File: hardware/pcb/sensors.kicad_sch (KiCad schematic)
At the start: 31 parts, among them J4 4-20mA_1, J5 4-20mA_2, J6 DS18B20, J7 Spare, Q2 BSS123, U9 ADS1115

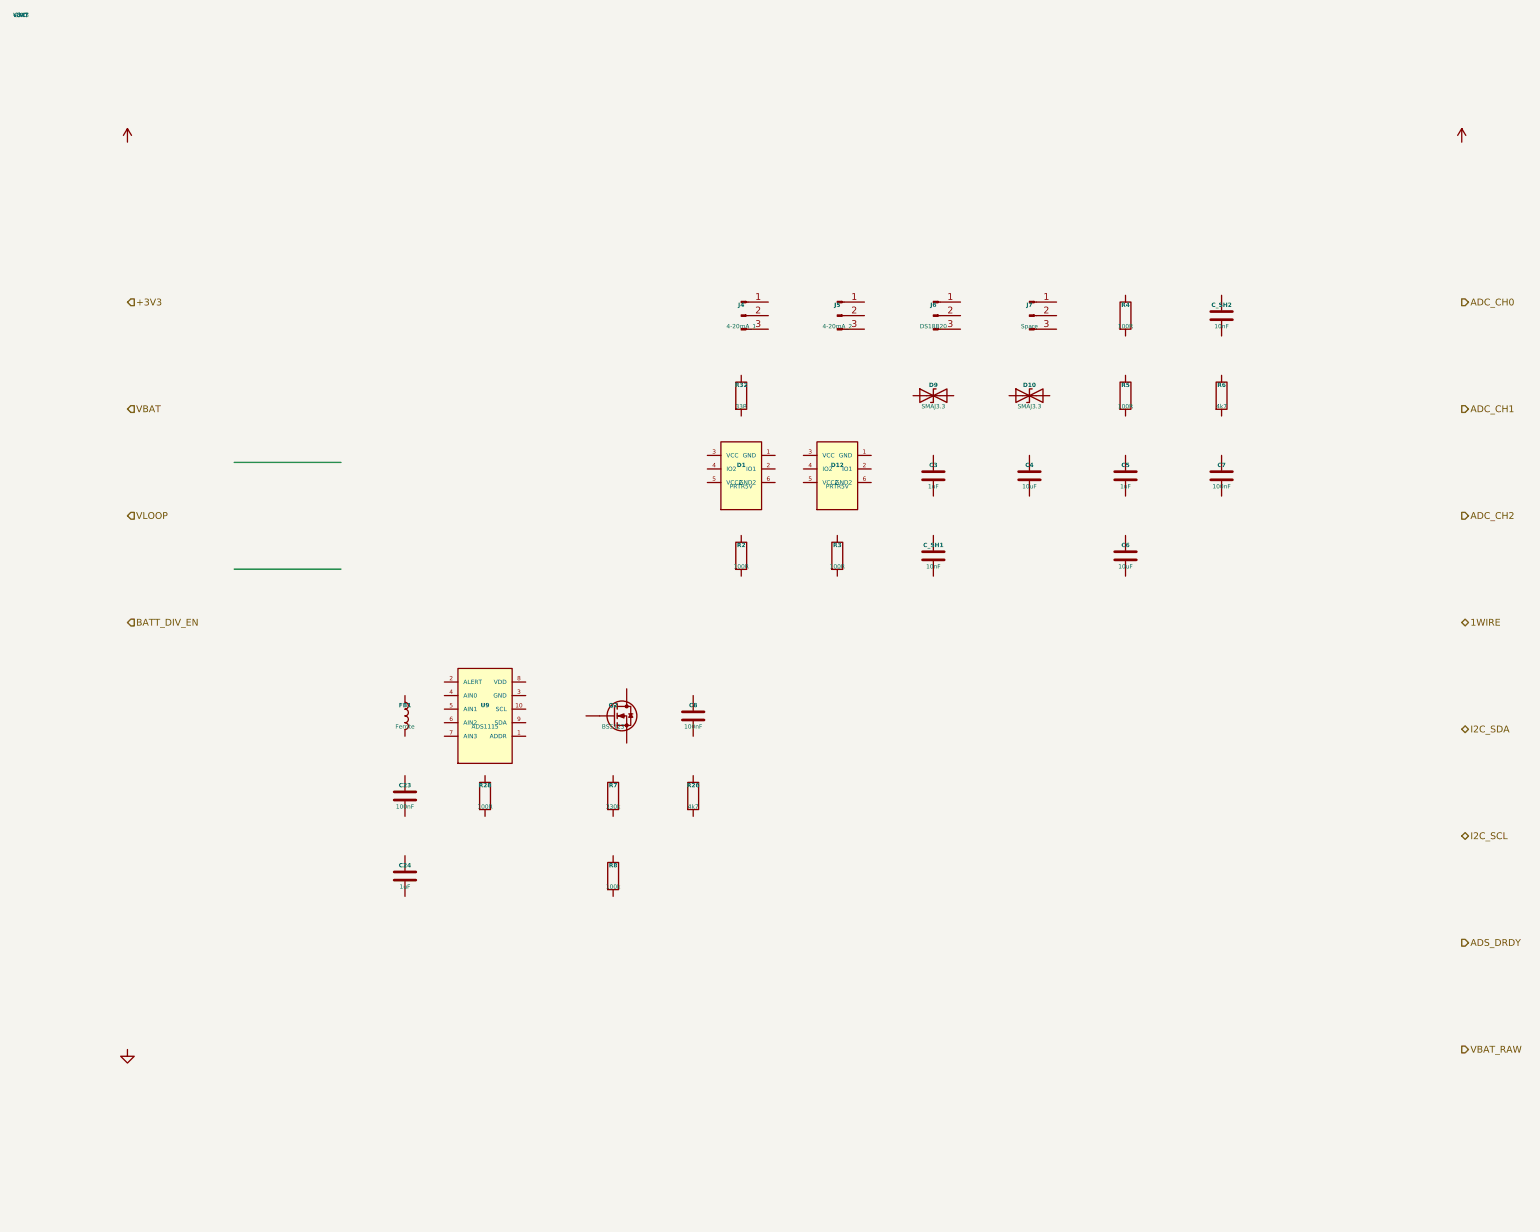
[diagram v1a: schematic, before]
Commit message: fix(sch): eliminate all structural ERC violations in hierarchical schematic
Three root causes fixed in generate_kicad.py:

1. Left-side sheet pins used angle=0 — kicad-cli upgrade snapped them to
   the right border, colliding with right-side pins and causing
   multiple_net_names and unconnected_wire_endpoint. Fixed: px==0 pins
   now use angle=180 (outward-left), px>0 pins keep angle=0.

2. Subsheet hierarchical labels and power symbols were at off-grid
   positions (20 mm, 50 mm, 70 mm, …). Replaced with 1.27 mm-aligned
   values (25.4, 50.8, 63.5, … multiples of 500 mil).

3. _remap_positions() produced arbitrary floats. Added _snap() that
   rounds every remapped coordinate to the nearest 1.27 mm grid point,
   eliminating component-pin endpoint_off_grid violations.

Also: paper size bumped A3 → A2 (layout reaches y ≈ 407 mm, exceeding
A3 height of 297 mm). SHEETS definition pinned to 1.27 mm-aligned
origins and heights; MCU left-side pins reordered to match power
right-side y-levels for direct horizontal wires.

ERC result: 588 → 404 violations.
Eliminated: endpoint_off_grid (−129), unconnected_wire_endpoint (−4),
wire_dangling (−2), multiple_net_names (−1).
Remaining 404 are structural (pin_not_connected, label_dangling) that
require full intra-sheet wiring — not addressable by the generator alone.

Netlist unchanged: 118 refs, 34 nets.

Co-Authored-By: Claude Sonnet 4.6 <noreply@anthropic.com>
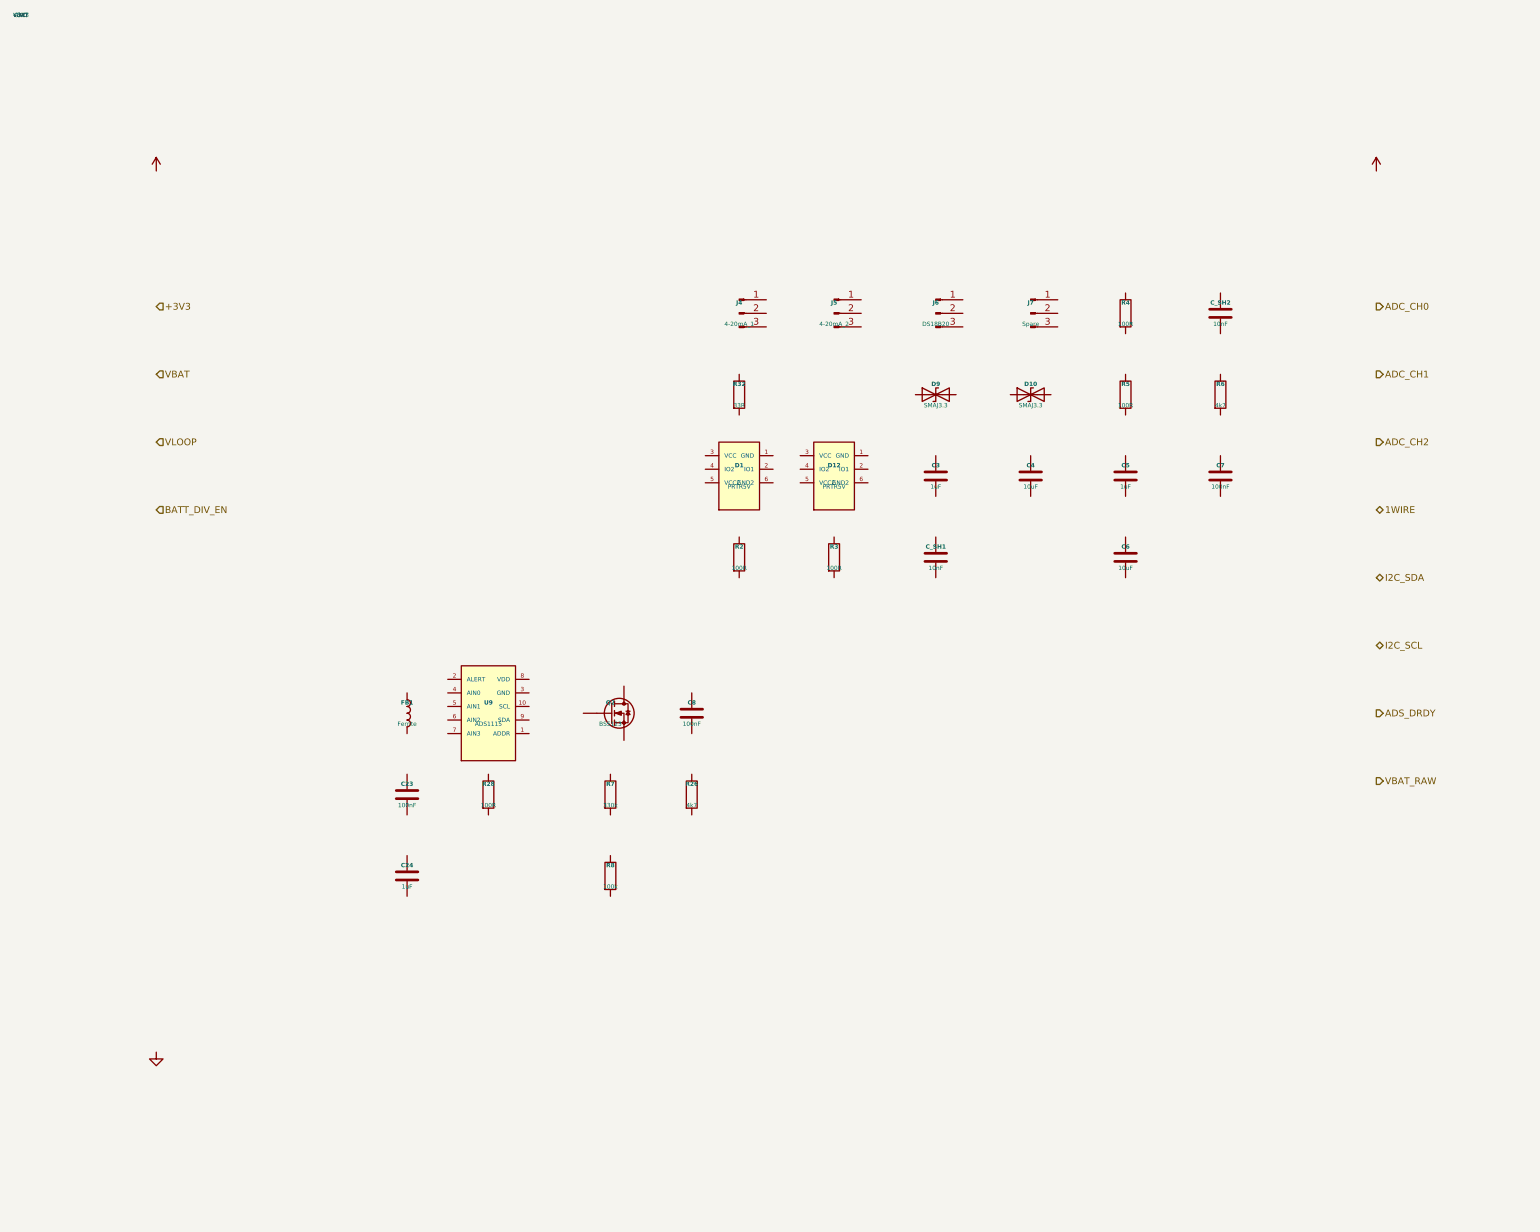
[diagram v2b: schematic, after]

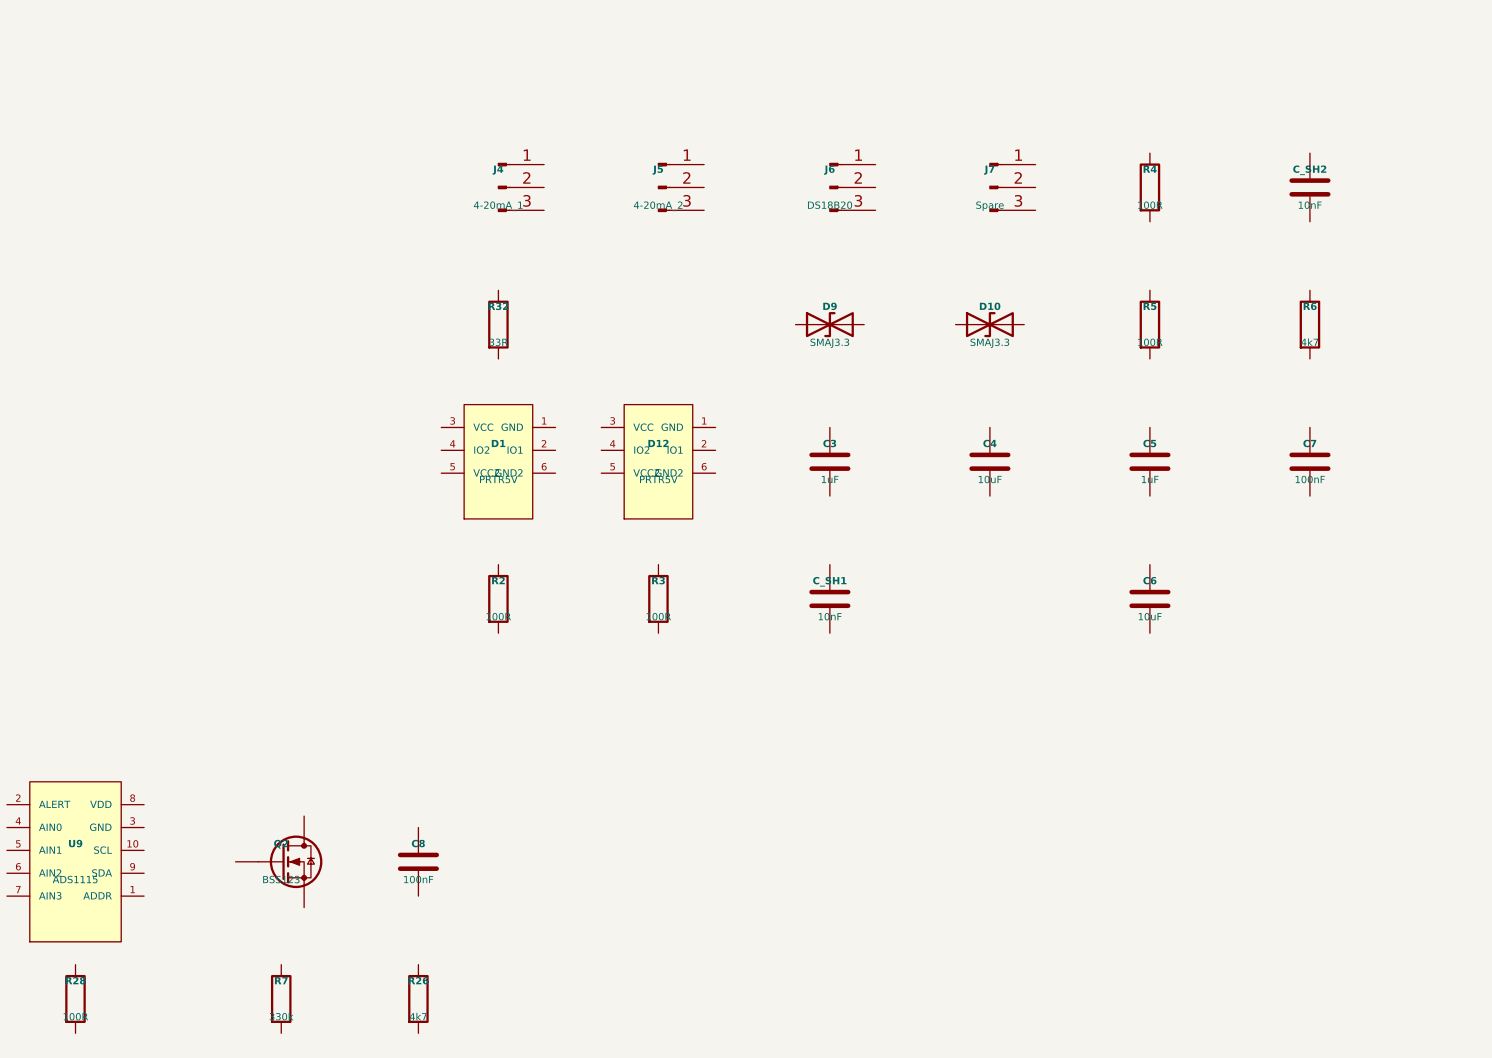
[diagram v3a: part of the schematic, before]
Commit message: hw(pcb): fresh-start PCB — fix 4 critical schematic gaps, add wiring/placement docs
Archive old auto-generated PCB to hardware/pcb_old/. Start clean hardware/pcb/
with reference-only design documents for manual KiCad layout.

Critical electrical fixes:
- Add R_FBH (560kΩ) and R_FBL (124kΩ) symbols to power.kicad_sch — AP63205WU
  was missing its FB divider entirely; without it VOUT floats to rail and destroys
  the ESP32 on first power-on. Sets VOUT = 3.31V.
- Add R_DRDY (4.7kΩ) symbol to sensors.kicad_sch — ADS1115 ALERT/DRDY is
  open-drain and required an external pull-up; firmware was missing edges
  intermittently (root cause of bug fixed in adf7101).
- Add C_BST (100nF) symbol to power.kicad_sch — MT3608B BST→SW bootstrap
  cap is mandatory for gate driver; was ambiguous/missing.
- Add C_BUCK (10µF 0805) symbol to power.kicad_sch — AP63205WU primary output
  filter cap was absent from schematic.
- R33 already corrected from 604kΩ → 590kΩ (CN3722 CV 8.48V → 8.31V, safe for 2S).

New reference documents:
- bom_footprints.md — full BOM with KiCad 10 footprints, LCSC codes, PCBWay notes
- placement_constraints.md — must-be-near/apart rules from datasheets
- schematic_connections.md — net-by-net pin connectivity (authoritative wiring ref
  because schematic has symbols but zero wire connections yet)
- kicad_guide_eli5.md — step-by-step KiCad 10 setup guide including scripting console
- kicad_place_script.py — PCB editor scripting console auto-placement script
- senior_review_2026-05-25.md — senior reviewer report (BLOCKED, 4 CRITICAL)

CLAUDE.md: add electrical correctness gate to /improve cycle to catch missing
companion passives before tape-out.

Co-Authored-By: Claude Sonnet 4.6 <noreply@anthropic.com>
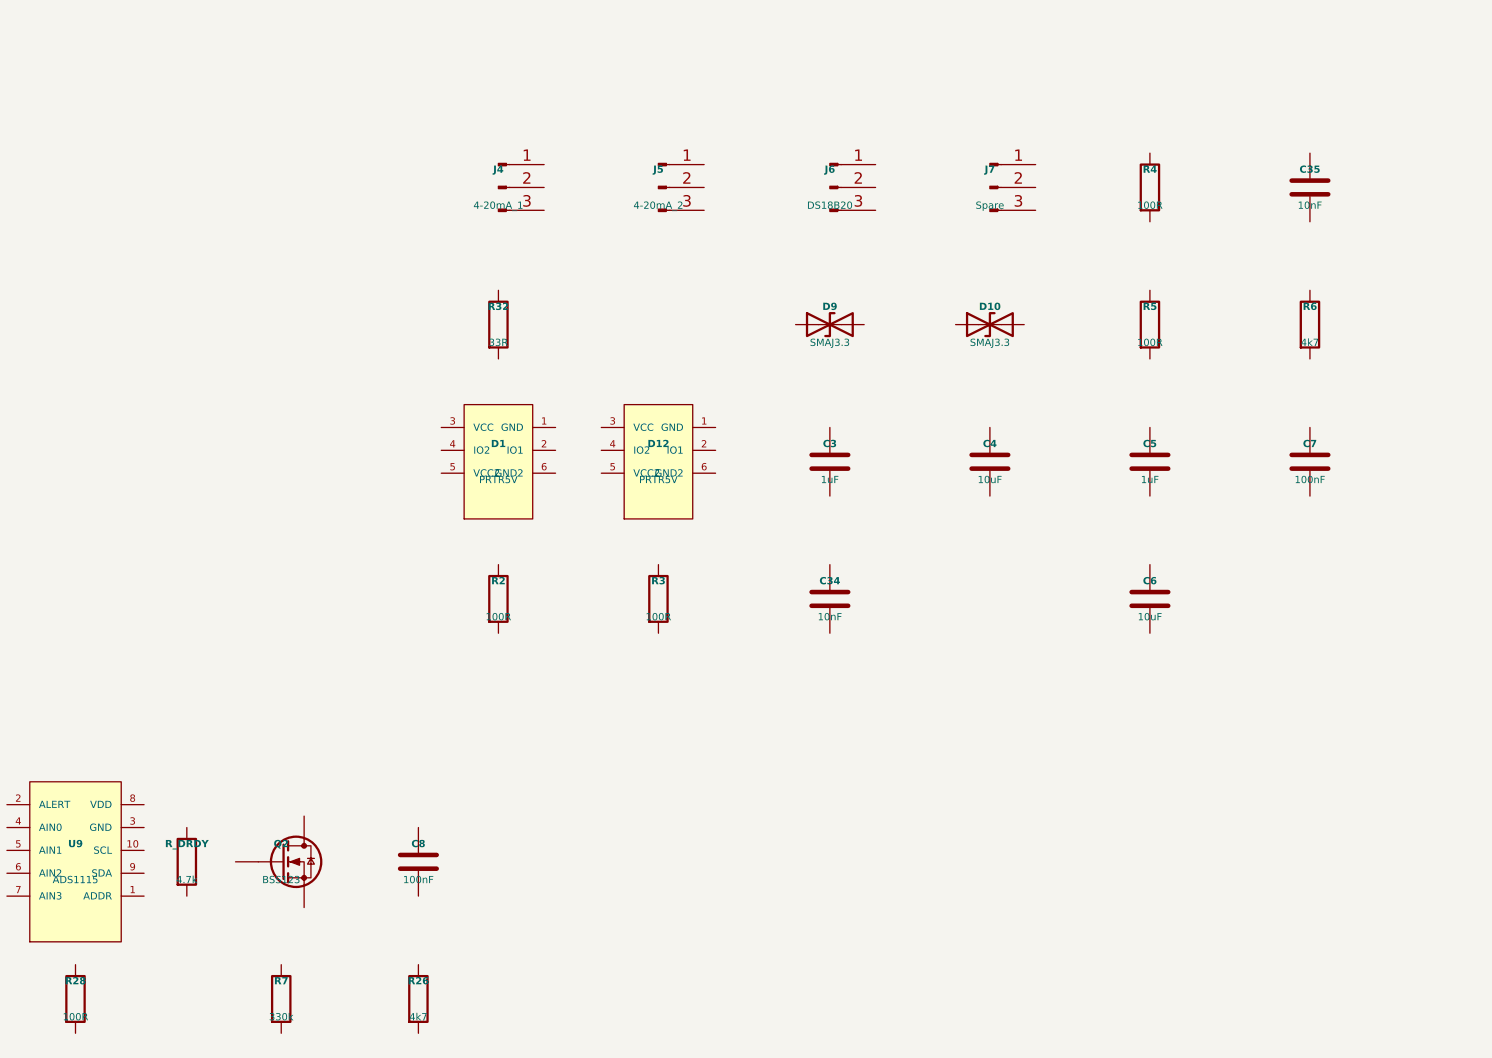
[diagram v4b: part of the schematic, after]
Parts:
- removed C_SH1, C_SH2: 10nF, Capacitor_SMD:C_0402_1005Metric, symbol Device:C
- added C34, C35: 10nF, Capacitor_SMD:C_0402_1005Metric, symbol Device:C
- added R_DRDY: 4.7k, Resistor_SMD:R_0402_1005Metric, symbol Device:R

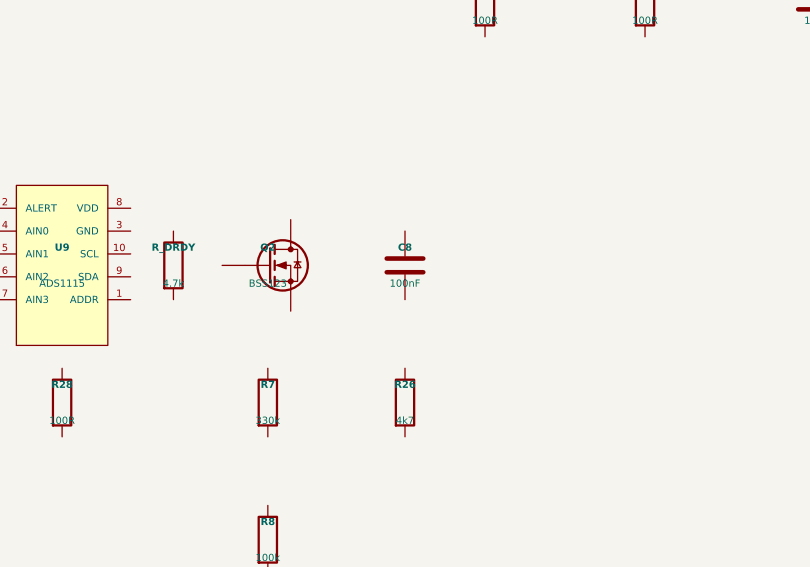
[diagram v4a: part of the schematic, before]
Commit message: hw(pcb): symbol pass — all parts placed, CN3722 redrawn TSSOP-16, CV/MPPT reference bug fixed
Clears the layout gate from senior_review_2026-07-06.md (CRITICALs 1-3)
and fixes a newly found CRITICAL:

- CN3722 CV divider was computed with the CN3791's 1.205 V reference;
  the CN3722's FB reference is 2.416 V (datasheet Rev 1.1, p.4), so the
  documented 590k/100k divider would regulate the 2S pack at ~16.7 V.
  R33 590k -> 243k (8.287 V; formula V_REG = 2.416 x (1 + Rh/Rl) stated
  at every location). Same root cause in the MPPT divider: ref is
  1.04 V, not 1.205 V — old values set the tracking point at 4.8 V,
  below the chip's 7.5 V minimum VCC; R20 36k -> 158k (V_MP ~17.5 V for
  a 12 V-nominal panel, flagged for recompute against the real panel).
- CN3722 symbol redrawn as the real TSSOP-16 (was an 8-pin fiction with
  a nonexistent VPROG pin); full external buck stage placed: M_SOLAR
  P-FET, D16 series + D_SOLAR catch Schottkys, L_SOLAR 47uH, R19
  repurposed as the 0.4R CSP-BAT sense resistor (500 mA), VG cap,
  COM1/2/3 compensation network, RT_SOLAR 10k NTC on TEMP (solar-path
  cold-charge cutoff — review finding O-1 closed for both chargers).
- IP2326 drawn as the verified 24-pin+EPAD part replacing TP5100
  (R36/R37 instances deleted), with R_VSET 120k, RISET 90k, L3 2.2uH,
  RT1 NTC, BST/VSYS caps. Footprint welld:IP2326_TBD pending the LCSC
  package code.
- MT3608B symbol numbering fixed to the standard family map
  (SW=1/GND=2/FB=3/EN=4/IN=5/NC=6; bench-verify note added — datasheet
  fetch was proxy-blocked).
- All previously missing symbols placed: D15, Q3/R29, Q4/R27, Q5/R16,
  R25 (power); R15/C36 EN RC, TP13 (mcu). Values synced: D8/D14
  SMAJ24CA, C8 1nF, C17 35V/1206, F2 2A-hold PTC.
- schematic_connections.md resolution/blocker tables updated; sheets
  still have no drawn wires — the doc remains the wiring authority
  until the wiring pass.

Co-Authored-By: Claude Fable 5 <noreply@anthropic.com>
Claude-Session: https://claude.ai/code/session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
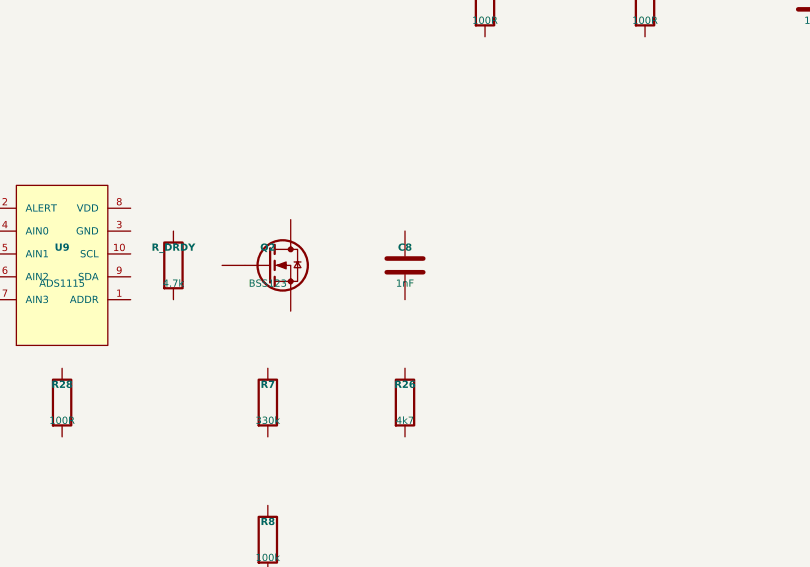
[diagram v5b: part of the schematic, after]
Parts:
- C8: value 100nF -> 1nF
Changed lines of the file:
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@@
 			)
 		)
-		(property "Value" "100nF"
+		(property "Value" "1nF"
 			(at 125.73 129 0)
 			(show_name no)
